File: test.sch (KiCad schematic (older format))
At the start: 168 parts, among them J1 microSD, J2 GNIAZDO_MODULU_1, J3 GNIAZDO_MODULU_2, J4 GNIAZDO_MODULU_3, J5 GNIAZDO_MODULU_4, J6 GNIAZDO_MODULU_5, J7 GNIAZDO_MODULU_6, P1 Gniazdo akumulatora, P7 Gniazdo akumulatora, P8 Gniazdo programatora SWD, T1 IRLML6401, T10 BSS138, T11 BSS138, T12 BSS138, T13 BSS138, T14 FDV304P, T2 IRLML6401, T3 IRLML6401, T4 IRLML6401, T5 IRLML6401, T6 IRLML6401, T7 BSS138, T8 BSS138, T9 BSS138, U1 MCP1755T-3302E/DC, U10 74LVX373M, U11 DHT22, U12 MIC29302, U13 S25FL1275ABMGI101, U14 DS3231SN, U15 ESP-07, U16 M590E, U17 SIMHOLDER, U18 TPS3823, U2 STM32F103C8, U3 MCP1755T-3302E/DC, U4 MCP1755T-3302E/DC, U5 MCP1755T-3302E/DC, U6 MCP1755T-3302E/DC, U7 MCP1755T-3302E/DC, U8 MCP1755T-3302E/DC, U9 74LVX373M, Y1 32768, Y2 14.7456 MHz

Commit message: wersja rev. 1.0
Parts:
- removed C13, C14, C15: 1u, Capacitors_SMD:C_0603, symbol C
- removed D2: LED_ALT, symbol LED_ALT
- removed F7: 1A, symbol Fuse_Small
- removed J7: GNIAZDO_MODULU_6, symbol GNIAZDO_MODULU_X
- removed R25, R26, R27, R28: 100k, Resistors_SMD:R_0603, symbol R
- removed U7: MCP1755T-3302E/DC, symbol MCP1755T-3302E/DC
- added C1, C2, C9: 1u, Capacitors_SMD:C_0603, symbol C
- added C33: 100p, Capacitors_SMD:C_0603, symbol C
- added D2, D3: LED, symbol LED
- added F1: 1A, symbol Fuse_Small
- added J1: GNIAZDO_MODULU_1, symbol GNIAZDO_MODULU_X
- added R1, R13, R14, R15, R16, R17, R18, R3, R4, R5, R6: 1k, Resistors_SMD:R_0603, symbol R
- added R10, R11, R12, R8, R9: 100k, Resistors_SMD:R_0603, symbol R
- added R37: 200, Resistors_SMD:R_0603, symbol R
- added R45: 680, Resistors_SMD:R_0603, symbol R
- added U2: MCP1755T-3302E/DC, symbol MCP1755T-3302E/DC
- C39: renamed from C42; value 1n -> 100p
- J2: value GNIAZDO_MODULU_1 -> GNIAZDO_MODULU_2
- J3: value GNIAZDO_MODULU_2 -> GNIAZDO_MODULU_3
- J4: value GNIAZDO_MODULU_3 -> GNIAZDO_MODULU_4
- J5: value GNIAZDO_MODULU_4 -> GNIAZDO_MODULU_5
- J6: value GNIAZDO_MODULU_5 -> GNIAZDO_MODULU_6
- R2: value 100k -> 1k
- U9: renamed from U2; symbol STM32F103C8-RESCUE-test -> STM32F103C8
- renumbered C32 to C13, C33 to C14, C18 to C15, C2 to C16, C34 to C17, C16 to C18, C17 to C19, C19 to C20, C20 to C21, C35 to C22, C36 to C23, C21 to C24, C22 to C25, C23 to C26, C1 to C27, C24 to C28, C9 to C29, C25 to C30, C37 to C31, C26 to C32, C44 to C34, C27 to C35, C39 to C36, C38 to C37, C40 to C38, C41 to C40, C28 to C41, C43 to C42, C29 to C43, C30 to C44, C31 to C45, F1 to F7, F9 to F8, F8 to F9, J1 to J7, P7 to P1, P1 to P2, P8 to P3, R39 to R25, R1 to R26, R29 to R27, R30 to R28, R31 to R29, R32 to R30, R33 to R31, R3 to R32, R4 to R33, R5 to R34, R6 to R35, R8 to R36, R34 to R38, R35 to R39, R36 to R40, R9 to R41, R10 to R42, R11 to R43, R12 to R44, R13 to R46, R14 to R47, R37 to R48, R38 to R49, R17 to R50, R15 to R51, R16 to R52, R18 to R53, TP25 to TP13, TP26 to TP14, TP27 to TP19, TP28 to TP21, TP19 to TP22, TP21 to TP23, TP13 to TP24, TP14 to TP25, TP22 to TP26, TP23 to TP27, TP24 to TP28, U8 to U10, U12 to U11, U18 to U12, U11 to U13, U16 to U15, U13 to U16, U15 to U17, U17 to U18, U9 to U7, U10 to U8
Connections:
- wire segments 702 -> 593
- no-connect marks 16 -> 27
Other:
- moved on the sheet: C14, C30, C32, R33, R34, R35, R36, R38, R43, R44, TP13, TP14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

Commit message: proba BOK i footprinty
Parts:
- F1: footprint (none) -> Resistors_SMD:R_0603_HandSoldering; Nazwa bezpiecznika (none) -> FUSE 0603-FF PW 1A0
- T1, T2, T3, T4, T5, T6: footprint (none) -> TO_SOT_Packages_SMD:SOT-23; symbol P-MOSFET -> IRLML6401
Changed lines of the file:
@@
 Data
 89 50 4E 47 0D 0A 1A 0A 00 00 00 0D 49 48 44 52 00 00 01 53 00 00 00 B1 08 02 00 00 00 F6 D2 C9
-1E 00 00 00 03 73 42 49 54 08 08 08 DB E1 4F E0 00 00 00 09 70 48 59 73 00 00 0E C3 00 00 0E C3
-01 C7 6F A8 64 00 00 20 00 49 44 41 54 78 9C EC BD 69 90 5C D9 75 26 F6 9D 73 EF 7D 99 55 E8 66
+1E 00 00 00 03 73 42 49 54 08 08 08 DB E1 4F E0 00 00 00 09 70 48 59 73 00 00 0E 74 00 00 0E 74
+01 6B 24 B3 D6 00 00 20 00 49 44 41 54 78 9C EC BD 69 90 5C D9 75 26 F6 9D 73 EF 7D 99 55 E8 66
 EF 6C 76 53 4D AA C9 6E 92 A2 B8 36 37 89 94 B8 8A A2 2D 6B C2 1E 53 96 65 CB 11 9A 3F 8E 19 C9
 0E 87 A5 70 84 BC 88 B6 14 61 87 1C 13 31 3F E6 D7 44 D8 61 8F 64 5B 9A 11 A9 E1 D6 EC 8D 8D 5E
@@
 F 0 "F1" H 1600 1015 50  0000 C CNN
 F 1 "1A" H 1600 1135 50  0000 C CNN
-F 2 "" H 1600 1075 50  0001 C CNN
+F 2 "Resistors_SMD:R_0603_HandSoldering" H 1600 1075 50  0001 C CNN
 F 3 "" H 1600 1075 50  0000 C CNN
+F 4 "FUSE 0603-FF PW 1A0" H 1600 955 30  0001 C CNN "Nazwa bezpiecznika"
 	1    1600 1075
 	1    0    0    -1
@@
 $EndComp
 $Comp
-L P-MOSFET T1
+L IRLML6401 T1
 U 1 1 594A6156
 P 2350 1075
 F 0 "T1" V 2200 1050 50  0000 R CNN
 F 1 "IRLML6401" V 2500 925 50  0000 L CNN
-F 2 "" H 2350 1075 60  0001 C CNN
+F 2 "TO_SOT_Packages_SMD:SOT-23" H 2350 1075 60  0001 C CNN
 F 3 "" H 2350 1075 60  0001 C CNN
 	1    2350 1075
@@
 $EndComp
 $Comp
-L P-MOSFET T2
+L IRLML6401 T2
 U 1 1 594A651D
 P 2350 2825
 F 0 "T2" V 2200 2800 50  0000 R CNN
 F 1 "IRLML6401" V 2500 2675 50  0000 L CNN
-F 2 "" H 2350 2825 60  0001 C CNN
+F 2 "TO_SOT_Packages_SMD:SOT-23" H 2350 2825 60  0001 C CNN
 F 3 "" H 2350 2825 60  0001 C CNN
 	1    2350 2825
@@
 $EndComp
 $Comp
-L P-MOSFET T3
+L IRLML6401 T3
 U 1 1 594A7D1A
 P 2350 4650
 F 0 "T3" V 2200 4625 50  0000 R CNN
 F 1 "IRLML6401" V 2500 4500 50  0000 L CNN
-F 2 "" H 2350 4650 60  0001 C CNN
+F 2 "TO_SOT_Packages_SMD:SOT-23" H 2350 4650 60  0001 C CNN
 F 3 "" H 2350 4650 60  0001 C CNN
 	1    2350 4650
@@
 $EndComp
 $Comp
-L P-MOSFET T4
+L IRLML6401 T4
 U 1 1 594A7DE1
 P 2350 6400
 F 0 "T4" V 2200 6375 50  0000 R CNN
 F 1 "IRLML6401" V 2500 6250 50  0000 L CNN
-F 2 "" H 2350 6400 60  0001 C CNN
+F 2 "TO_SOT_Packages_SMD:SOT-23" H 2350 6400 60  0001 C CNN
 F 3 "" H 2350 6400 60  0001 C CNN
 	1    2350 6400
@@
 $EndComp
 $Comp
-L P-MOSFET T5
+L IRLML6401 T5
 U 1 1 594A92F4
 P 2350 8150
 F 0 "T5" V 2200 8125 50  0000 R CNN
 F 1 "IRLML6401" V 2500 8000 50  0000 L CNN
-F 2 "" H 2350 8150 60  0001 C CNN
+F 2 "TO_SOT_Packages_SMD:SOT-23" H 2350 8150 60  0001 C CNN
 F 3 "" H 2350 8150 60  0001 C CNN
 	1    2350 8150
@@
 $EndComp
 $Comp
-L P-MOSFET T6
+L IRLML6401 T6
 U 1 1 594A93BB
 P 2350 9900
 F 0 "T6" V 2200 9875 50  0000 R CNN
 F 1 "IRLML6401" V 2500 9750 50  0000 L CNN
-F 2 "" H 2350 9900 60  0001 C CNN
+F 2 "TO_SOT_Packages_SMD:SOT-23" H 2350 9900 60  0001 C CNN
 F 3 "" H 2350 9900 60  0001 C CNN
 	1    2350 9900

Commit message: dodałem niektóre footprinty
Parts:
- BT1: footprint (none) -> footprints:CONNFLY_DS1092-13-N8S; Oznaczenie producenta (none) -> CONNFLY DS1092-13-N8S
- F10: value 10mA -> 63mA; footprint (none) -> footprints:SCHURTER_BEZPIECZNIK_OMF63_7.4x3.1; Nazwa bezpiecznika (none) -> SCHURTER 3402.0003.11
- F2, F3, F4, F5, F6: footprint (none) -> Resistors_SMD:R_0603_HandSoldering; Nazwa bezpiecznika (none) -> FUSE 0603-FF PW 1A0
- F7, F8: value 6.5A -> 7A; footprint (none) -> Resistors_SMD:R_1206_HandSoldering
- F9: value 0.5A -> 250mA; footprint (none) -> Resistors_SMD:R_1206_HandSoldering; Nazwa bezpiecznika (none) -> SCHURTER 3413.0010.11
- T10, T11, T12, T13, T7, T8, T9: footprint (none) -> TO_SOT_Packages_SMD:SOT-23; symbol N-MOSFET -> BSS138
- T14: symbol P-MOSFET -> FDV304P
- TP1, TP10, TP11, TP12, TP13, TP14, TP15, TP16, TP17, TP18, TP19, TP2, TP20, TP21, TP22, TP23, TP24, TP25, TP26, TP27, TP28, TP3, TP4, TP5, TP6, TP7, TP8, TP9: footprint (none) -> Measurement_Points:Measurement_Point_Round-SMD-Pad_Big
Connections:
- no-connect marks 27 -> 28
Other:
- moved on the sheet: R32, R35

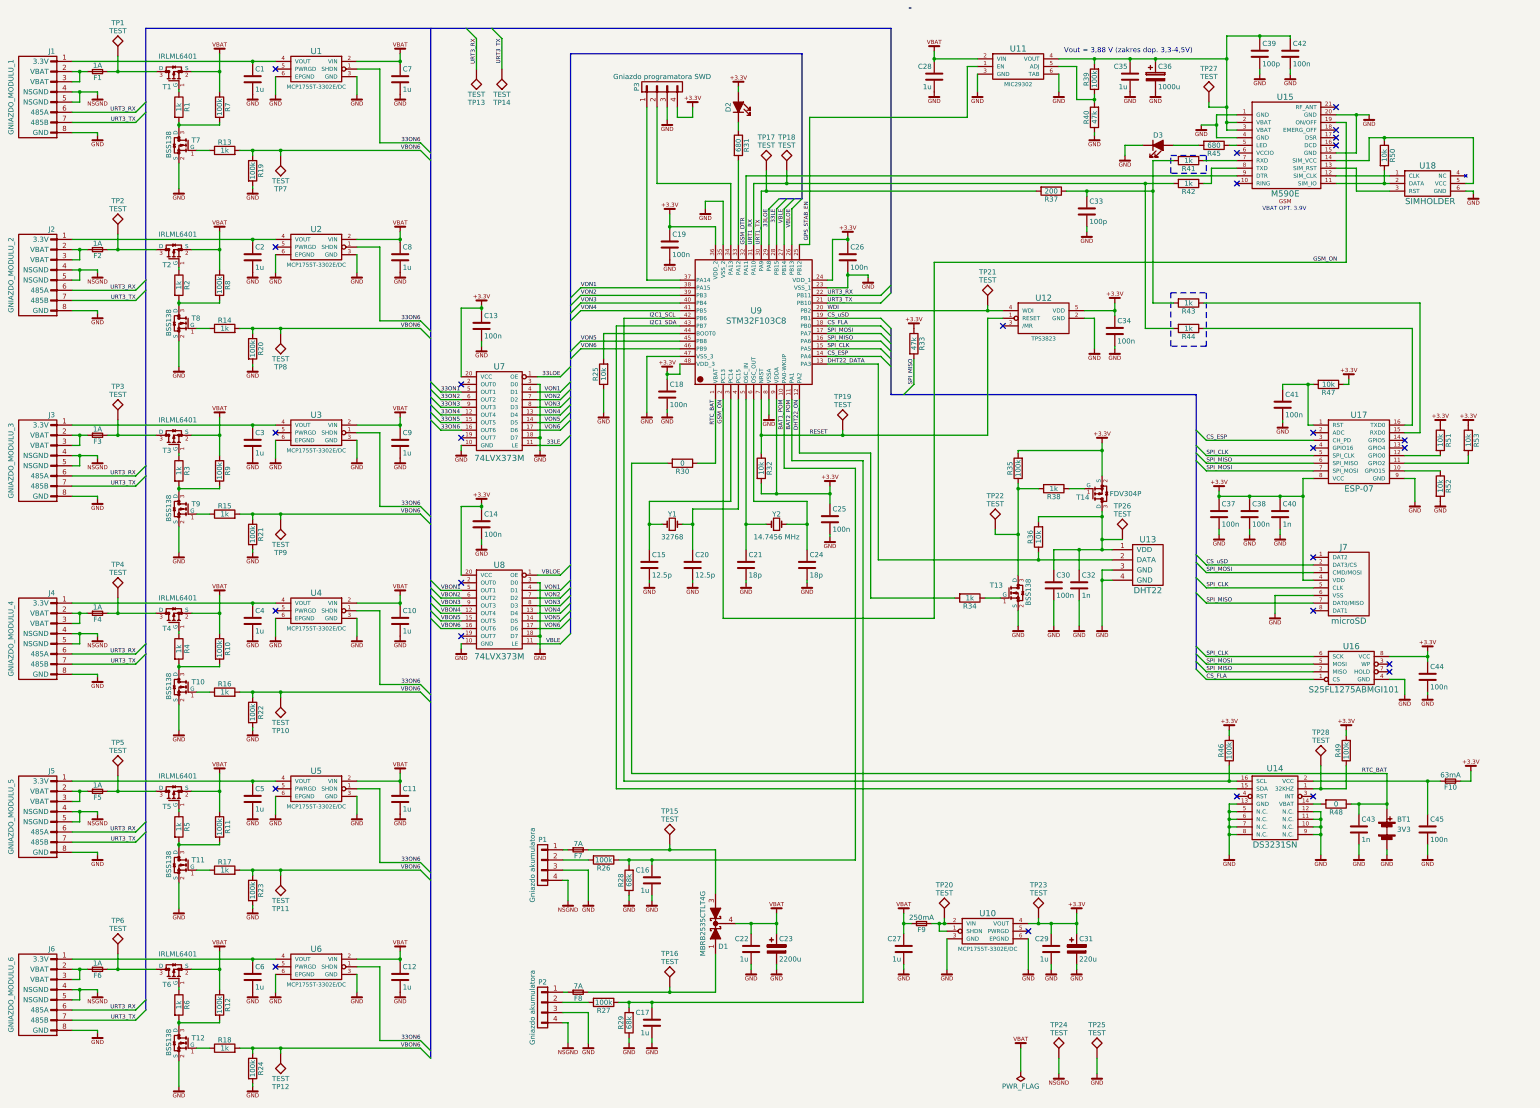
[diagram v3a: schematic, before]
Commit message: dodałem MAX3485
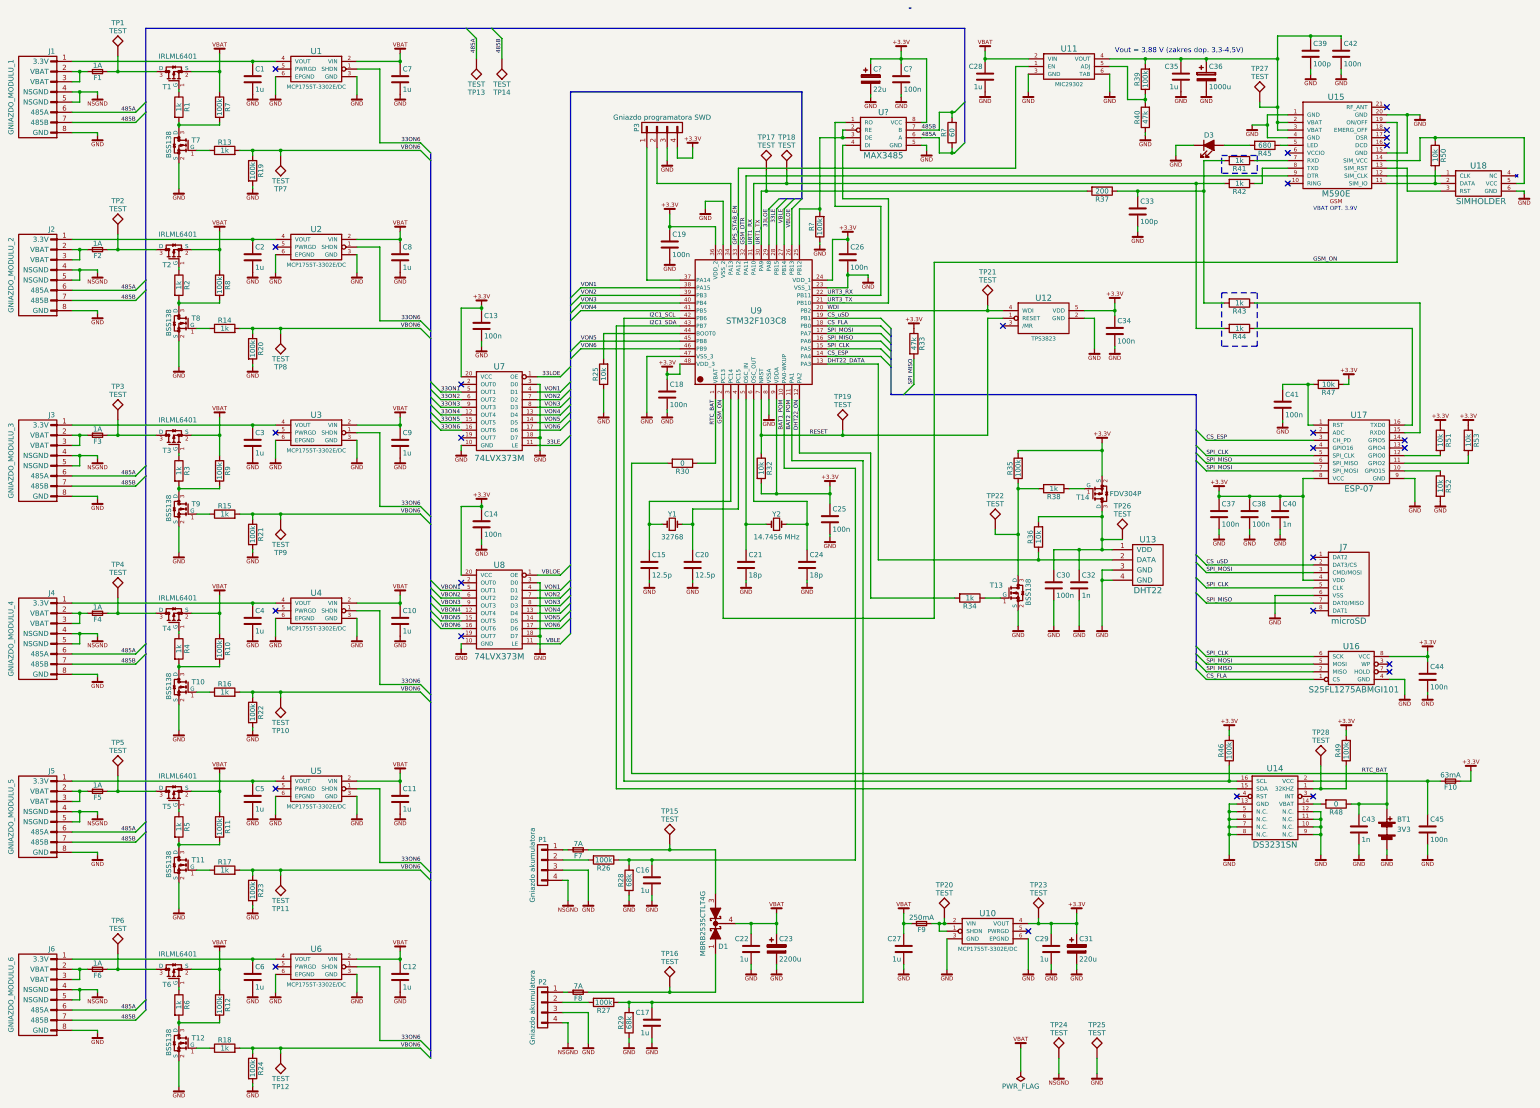
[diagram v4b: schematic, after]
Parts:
- removed D2: LED, symbol LED
- removed R31: 680, Resistors_SMD:R_0603, symbol R
- added C?: 100n, Capacitors_SMD:C_0603, symbol C
- added C?: 22u, symbol CP
- added R?: 60, Resistors_SMD:R_0603, symbol R
- added R?: 100k, Resistors_SMD:R_0603, symbol R
- added U?: MAX3485, Power_Integrations:SO-8, symbol MAX3485
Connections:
- net GPS_STAB_EN: now also U9.33 (PA12); no longer U9.25 (PB12)
- net URT3_RX: now also U?.1 (RO); no longer J1.6 (485A), J2.6 (485A), J3.6 (485A), J4.6 (485A), J5.6 (485A), J6.6 (485A), TP13.1
- net URT3_TX: now also U?.4 (DI); no longer J1.7 (485B), J2.7 (485B), J3.7 (485B), J4.7 (485B), J5.7 (485B), J6.7 (485B), TP14.1
- new net: R?.2, U9.25 (PB12), U?.2 (RE), U?.3 (DE)
- new net: C?.1, C?.1, U?.8 (VCC)
- new net 485A: J1.6 (485A), J2.6 (485A), J3.6 (485A), J4.6 (485A), J5.6 (485A), J6.6 (485A), R?.1, TP13.1, U?.6 (A)
- new net 485B: J1.7 (485B), J2.7 (485B), J3.7 (485B), J4.7 (485B), J5.7 (485B), J6.7 (485B), R?.2, TP14.1, U?.7 (B)
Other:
- moved on the sheet: C28, C33, C35, C36, C39, C42, D3, P3, R37, R39, R40, R41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

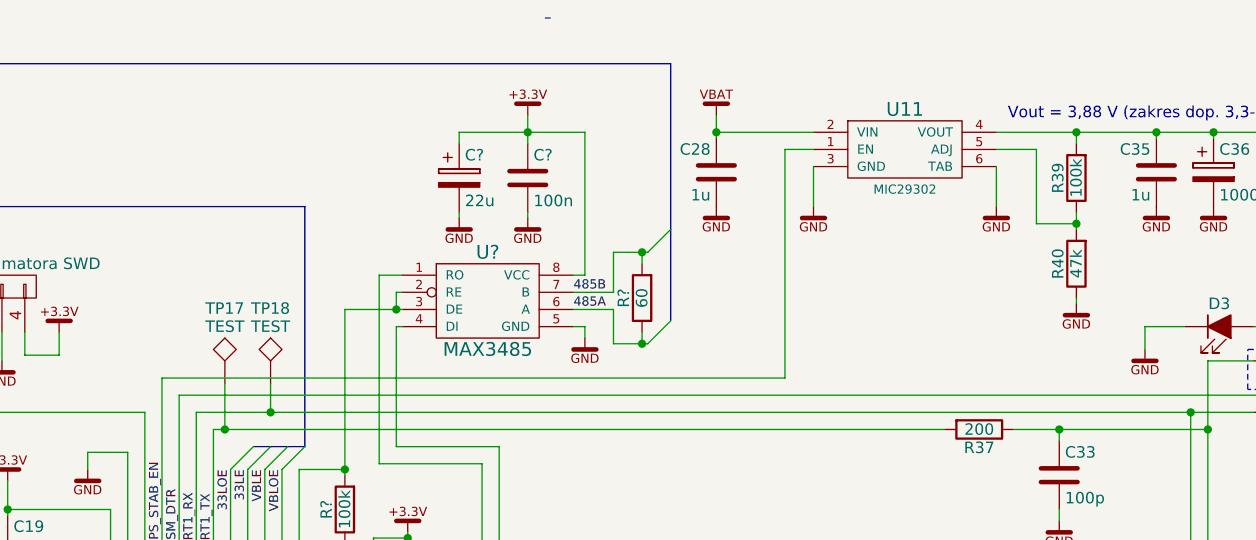
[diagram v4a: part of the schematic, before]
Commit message: footprint M590E
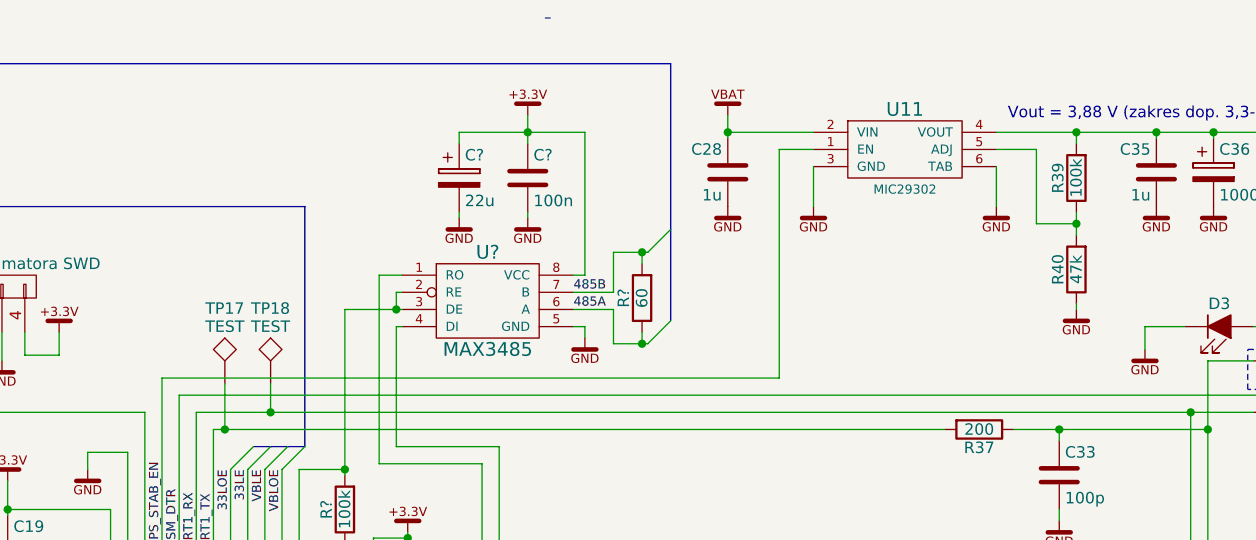
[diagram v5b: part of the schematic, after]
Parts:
- U15: footprint (none) -> footprints:M590E
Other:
- moved on the sheet: C28, R40

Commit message: dodałem footprint do ESP-07
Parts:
- U17: footprint (none) -> footprints:ESP-07
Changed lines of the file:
@@
 F 0 "U17" H 14000 5150 60  0000 C CNN
 F 1 "ESP-07" H 14000 4425 60  0000 C CNN
-F 2 "" H 13950 4975 60  0001 C CNN
+F 2 "footprints:ESP-07" H 13950 4975 60  0001 C CNN
 F 3 "" H 13950 4975 60  0001 C CNN
 	1    14000 4800

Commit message: footp
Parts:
- U1, U10, U2, U3, U4, U5, U6: footprint (none) -> TO_SOT_Packages_SMD:SOT-223-5
- U11: footprint (none) -> TO_SOT_Packages_SMD:TO-263-5_TabPin6
- U13: footprint (none) -> footprints:DHT22
- U14: footprint (none) -> SMD_Packages:SO-16-W
- U16: footprint (none) -> Power_Integrations:SO-8
- U7, U8: footprint (none) -> Housings_SOIC:SOIC-20W_7.5x12.8mm_Pitch1.27mm
- gave numbers to parts that had none: 5
